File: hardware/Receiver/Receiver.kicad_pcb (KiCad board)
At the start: 4 copper layers, 65 x 42 mm, 98 parts, among them IC1 ESP32-C3-MINI-1-N4, J1 USB_C_Receptacle_USB2.0, J4 Conn_01x03, J5 20021511-00006T4LF, J6 Conn_01x04, Q1 2N7002, SW1 Reset, SW2 1825027-8, U1 DMG6602SVTQ, U2 DMG6602SVTQ, U3 TLV493DA1B6HTSA2, U4 TPS22810DRV, U5 TPS22810DRV, U6 AZ1117-3.3

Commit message: Removed old files
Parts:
- moved H4 2.35 mm to (134.5, 84.5)
- moved H2 2.35 mm to (165.6, 84.5)

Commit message: Revision 1.2 of receiver board
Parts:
- removed C1: 0.1u, Capacitor_SMD:C_0402_1005Metric
- D3: value D -> 1N4148WQ-13-F; footprint Capacitor_SMD:C_0402_1005Metric -> Diode_SMD:D_SOD-123
- D5: value D_Schottky -> EVVO SS16; footprint Diode_SMD:D_SOD-128 -> Diode_SMD:D_SMA
- moved J5 52.6 mm to (127.0, 83.3), turned to 0 degrees
- moved R15 48.0 mm to (180.0, 113.2), turned to -90 degrees
- moved U6 42.4 mm to (172.3, 116.4), turned to -90 degrees
- moved R6 42.0 mm to (167.2, 111.6), turned to 180 degrees
- moved Q1 41.9 mm to (177.7, 112.2), turned to 90 degrees
- moved R7 40.4 mm to (165.2, 111.6)
- moved R10 39.7 mm to (163.5, 110.2), turned to 180 degrees
- moved R21 38.0 mm to (171.4, 107.1), turned to 180 degrees
- moved C27 37.6 mm to (173.4, 111.4), turned to 0 degrees
- moved U1 37.0 mm to (166.4, 108.9), turned to 90 degrees
- moved SW1 36.9 mm to (136.6, 110.5), turned to 180 degrees
- moved D5 36.1 mm to (176.7, 108.4), turned to 0 degrees
- moved C25 35.8 mm to (171.1, 111.4), turned to 0 degrees
- moved D3 35.8 mm to (161.1, 108.4), turned to 0 degrees
- moved R13 35.0 mm to (164.0, 108.6), turned to -90 degrees
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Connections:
- IC1 pad 10: /DN_BTN -> /SHUTDOWN
- IC1 pad 11: unconnected-(IC1-IO32-Pad11) -> /DIR
- IC1 pad 12: unconnected-(IC1-IO33-Pad12) -> /STEP
- IC1 pad 13: unconnected-(IC1-IO25-Pad13) -> /MOT_nRST
- IC1 pad 14: unconnected-(IC1-IO26-Pad14) -> /MS3
- IC1 pad 15: unconnected-(IC1-IO27-Pad15) -> /MS2
- IC1 pad 16: unconnected-(IC1-IO14-Pad16) -> /MS1
- IC1 pad 25: /STEP -> unconnected-(IC1-IO9-Pad25)
- IC1 pad 26: /MOT_nRST -> unconnected-(IC1-IO10-Pad26)
- IC1 pad 29: /DIR -> unconnected-(IC1-IO5-Pad29)
- IC1 pad 34: /ADDRS_LED -> unconnected-(IC1-IO21-Pad34)
- IC1 pad 5: /MS3 -> unconnected-(IC1-I37-Pad5)
- IC1 pad 6: /MS2 -> unconnected-(IC1-I38-Pad6)
- IC1 pad 7: /MS1 -> unconnected-(IC1-I39-Pad7)
- IC1 pad 9: /UP_BTN -> /ADDRS_LED
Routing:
- net /SHUTDOWN: track 3.31 -> 47.4 mm
- net GND: track 154.7 -> 112.9 mm, vias 90 -> 95
- net /VUSB: track 53.7 -> 93.9 mm, vias 2 -> 5
- net /VSYS: track 8.26 -> 34.9 mm, vias 15 -> 7
- net /ESP_RX: track 33.0 -> 9.15 mm, vias 1 -> 0
- net /ESP_TX: track 30.4 -> 10.9 mm, vias 1 -> 0
- net /MOT_nEN: track 24.8 -> 40.9 mm
- net /STEP: track 27.0 -> 41.6 mm
- net /MS1: track 19.3 -> 33.6 mm
- net /MS2: track 19.6 -> 33.7 mm
- net /MS3: track 19.9 -> 33.8 mm
- net Net-(D3-K): track 25.9 -> 12.1 mm, vias 1 -> 0
- net /DIR: track 29.1 -> 42.8 mm
- net /SCL: track 13.4 -> 26.9 mm
- net /CNTRL: track 17.0 -> 6.09 mm, vias 4 -> 0
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- added copper zone on F.Cu, net +3.3V
- added copper zone on F.Cu, net /VIN
- removed copper zone on B.Cu, net /VSYS
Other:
- board text added: "JLCJLCJLCJLC"
- board text added: "REV 1.2.0"
- board text added: "STATUS"
- board text removed: "RESET"
- board text removed: "REV 1.0.0"

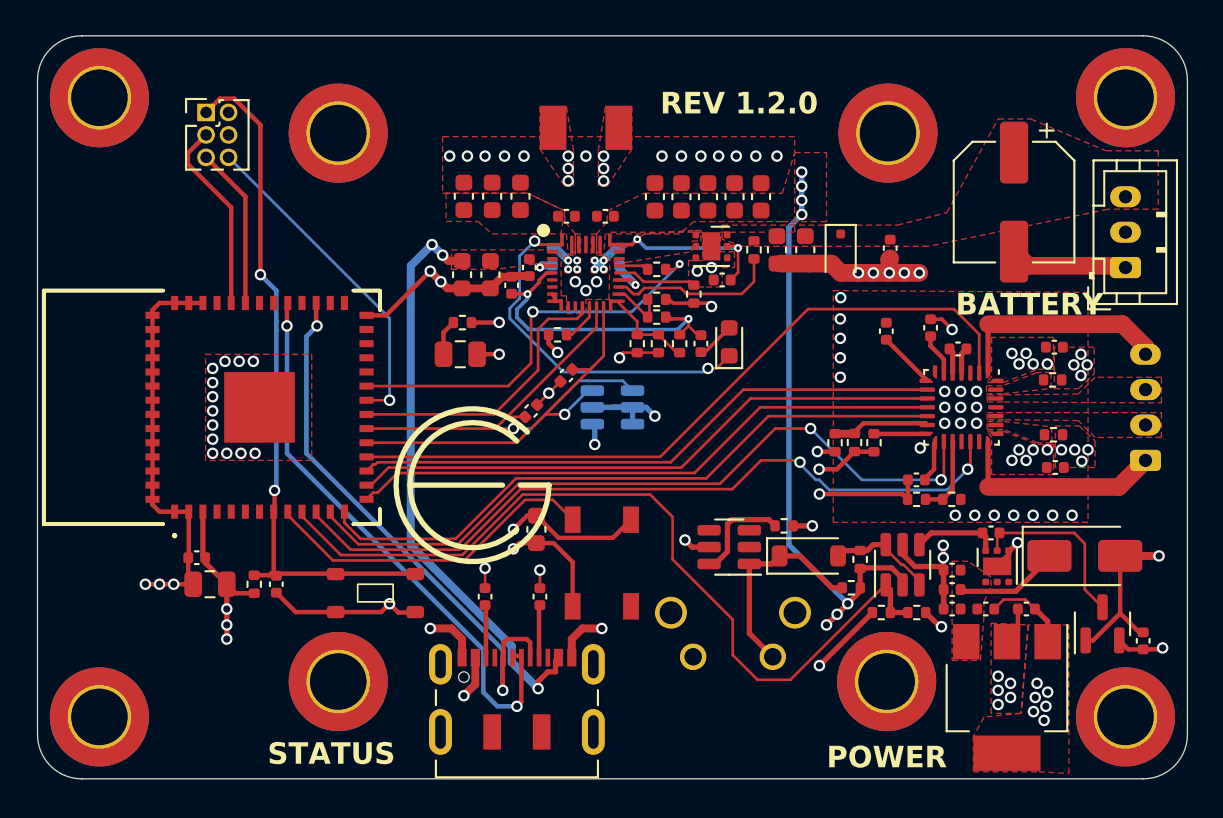
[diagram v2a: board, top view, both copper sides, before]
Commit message: BMS added to hardware
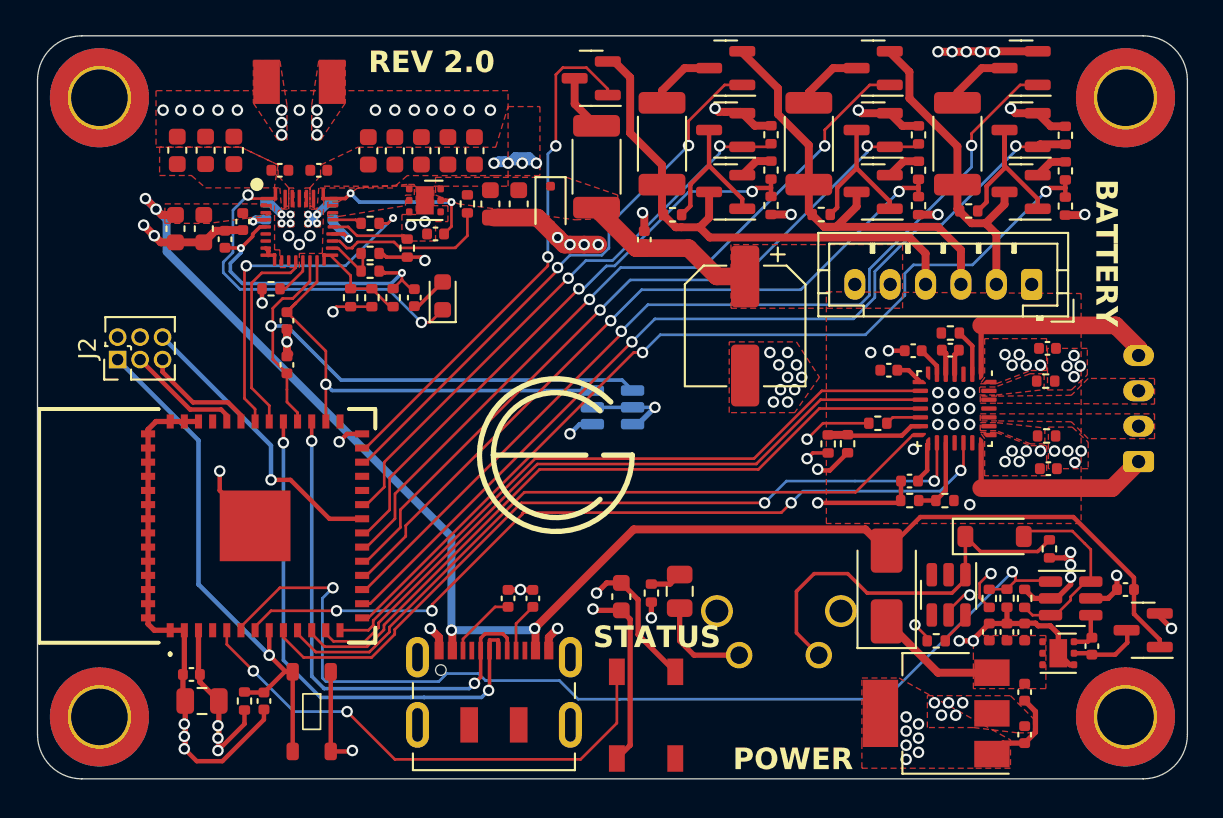
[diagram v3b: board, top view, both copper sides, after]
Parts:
- removed the C27 at (173.4, 111.4)
- removed the C32 at (126.5, 108.5)
- removed the C34 at (131.0, 110.0)
- removed the C7 at (145.7, 106.9)
- removed the D3 at (161.1, 108.4)
- removed the D5 at (176.7, 108.4)
- removed the H1 at (165.5, 115.5)
- removed the H2 at (165.6, 84.5)
- removed the H3 at (134.5, 115.5)
- removed the H4 at (134.5, 84.5)
- removed the J4 at (179.0, 92.1)
- removed J5: 20021511-00006T4LF, Connector_PinHeader_1.27mm:PinHeader_2x03_P1.27mm_Vertical
- removed the R10 at (163.5, 110.2)
- removed the R12 at (159.7, 106.7)
- removed the R13 at (164.0, 108.6)
- removed the R15 at (180.0, 113.2)
- removed the R2 at (142.8, 110.7)
- removed the R3 at (145.9, 110.7)
- removed the U1 at (166.4, 108.9)
- removed the U4 at (171.8, 109.0)
- added C21: 10u, Capacitor_SMD:C_0402_1005Metric, F.Cu at (173.3, 112.7)
- added C29: 47u, Capacitor_SMD:CP_Elec_6.3x5.4, F.Cu at (157.5, 95.4)
- added C33: 1u, Capacitor_SMD:C_0402_1005Metric, F.Cu at (130.3, 116.6)
- added C6: 10u, Capacitor_SMD:C_0603_1608Metric, F.Cu at (150.5, 110.7)
- added D4: 1N4148WQ-13-F, Diode_SMD:D_SOD-123, F.Cu at (171.6, 107.3)
- added D6: EVVO SS16, Diode_SMD:D_SMA, F.Cu at (165.5, 110.1)
- added J2: 20021511-00006T4LF, Connector_PinHeader_1.27mm:PinHeader_2x03_P1.27mm_Vertical, F.Cu at (122.0, 97.3)
- added J3: JST_PH, Connector_JST:JST_PH_B6B-PH-K_1x06_P2.00mm_Vertical, F.Cu at (173.7, 93.0)
- added Q10: NChan, Package_TO_SOT_SMD:SOT-23, F.Cu at (164.7, 80.8)
- added Q11: NChan, Package_TO_SOT_SMD:SOT-23, F.Cu at (173.1, 80.8)
- added Q2: NChan, Package_TO_SOT_SMD:SOT-23, F.Cu at (156.4, 84.3)
- added Q3: NChan, Package_TO_SOT_SMD:SOT-23, F.Cu at (164.7, 84.3)
- added Q4: NChan, Package_TO_SOT_SMD:SOT-23, F.Cu at (173.1, 84.3)
- added Q5: PChan, Package_TO_SOT_SMD:SOT-23, F.Cu at (156.4, 87.8)
- added Q6: PChan, Package_TO_SOT_SMD:SOT-23, F.Cu at (164.7, 87.8)
- added Q7: PChan, Package_TO_SOT_SMD:SOT-23, F.Cu at (173.1, 87.8)
- added Q8: NChan, Package_TO_SOT_SMD:SOT-23, F.Cu at (148.8, 81.4)
- added Q9: NChan, Package_TO_SOT_SMD:SOT-23, F.Cu at (156.4, 80.8)
- added R11: 100k, Resistor_SMD:R_0402_1005Metric, F.Cu at (168.3, 113.2)
- added R17: 100k, Resistor_SMD:R_0402_1005Metric, F.Cu at (173.3, 110.8)
- added R19: 100k, Capacitor_SMD:C_0402_1005Metric, F.Cu at (179.0, 110.3)
- added R20: 100k, Capacitor_SMD:C_0402_1005Metric, F.Cu at (177.1, 113.5)
- added R22: 100k, Resistor_SMD:R_0402_1005Metric, F.Cu at (167.3, 84.6)
- added R27: 282k, Resistor_SMD:R_0402_1005Metric, F.Cu at (159.0, 86.6)
- added R28: 100k, Resistor_SMD:R_0402_1005Metric, F.Cu at (159.0, 88.6)
- added R29: 155k, Resistor_SMD:R_0402_1005Metric, F.Cu at (167.3, 86.6)
- added R30: 100k, Resistor_SMD:R_0402_1005Metric, F.Cu at (167.3, 88.6)
- added R31: 28k, Resistor_SMD:R_0402_1005Metric, F.Cu at (175.6, 86.6)
- added R32: 100k, Resistor_SMD:R_0402_1005Metric, F.Cu at (175.6, 88.6)
- added R33: 400, Resistor_SMD:R_2010_5025Metric, F.Cu at (149.1, 86.4)
- added R34: 400, Resistor_SMD:R_2010_5025Metric, F.Cu at (152.8, 85.1)
- added R35: 400, Resistor_SMD:R_2010_5025Metric, F.Cu at (161.1, 85.1)
- added R36: 400, Resistor_SMD:R_2010_5025Metric, F.Cu at (169.5, 85.1)
- added R37: 100k, Resistor_SMD:R_0402_1005Metric, F.Cu at (169.1, 95.8)
- added R38: 100k, Resistor_SMD:R_0402_1005Metric, F.Cu at (165.0, 100.9)
- added R39: 10k, Capacitor_SMD:C_0402_1005Metric, F.Cu at (131.6, 95.1)
- added R40: 10k, Capacitor_SMD:C_0402_1005Metric, F.Cu at (131.6, 97.6)
- added R41: 10k, Resistor_SMD:R_0402_1005Metric, F.Cu at (129.2, 116.6)
- added R5: 5.1k, Capacitor_SMD:C_0402_1005Metric, F.Cu at (145.5, 110.8)
- added R8: 1M, Resistor_SMD:R_0402_1005Metric, F.Cu at (172.3, 110.8)
- added R9: 100k, Resistor_SMD:R_0402_1005Metric, F.Cu at (174.7, 108.0)
- added U3: DMG6602SVTQ, Package_TO_SOT_SMD:TSOT-23-6, F.Cu at (169.0, 110.6)
- added U5: TPS22810DRV, Package_SON:WSON-6-1EP_2x2mm_P0.65mm_EP1x1.6mm, F.Cu at (175.2, 113.9)
- C22: value 10u -> 1u
- C23: value 1u -> 0.1u
- C24: value 0.1u -> 10u
- C25: value 10u -> 10uf
- C26: value 10uf -> 22u
- C30: value 47u -> 22u; footprint Capacitor_SMD:CP_Elec_6.3x5.4 -> Capacitor_SMD:C_0805_2012Metric
- C31: value 22u -> 0.1u; footprint Capacitor_SMD:C_0805_2012Metric -> Capacitor_SMD:C_0402_1005Metric
- R21: footprint Capacitor_SMD:C_0402_1005Metric -> Resistor_SMD:R_0402_1005Metric
- R24, R25: value 10k -> 100k; footprint Capacitor_SMD:C_0402_1005Metric -> Resistor_SMD:R_0402_1005Metric
- R26: value 10k -> 100k
- R4: footprint Resistor_SMD:R_0402_1005Metric -> Capacitor_SMD:C_0402_1005Metric
- R6: value 100k -> 5.1k
- R7: value 1M -> 100k
- moved C30 53.9 mm to (126.8, 116.6), turned to 180 degrees
- moved R26 45.6 mm to (170.1, 88.9), turned to 0 degrees
- moved C26 28.5 mm to (173.3, 118.5)
- moved C25 28.4 mm to (151.8, 90.5), turned to 90 degrees
- moved R21 25.7 mm to (159.0, 84.6), turned to 90 degrees
- moved R23 20.5 mm to (175.6, 84.6)
- moved R25 19.8 mm to (161.8, 89.1), turned to 0 degrees
- moved U2 19.5 mm to (175.9, 110.8), turned to 0 degrees
- moved D2 18.3 mm to (153.8, 110.4), turned to 90 degrees
- moved D5 16.6 mm to (146.5, 88.6)
- moved C10 16.4 mm to (128.6, 85.5)
- moved C7 16.4 mm to (131.2, 86.6)
- moved R1 16.4 mm to (130.7, 93.3), turned to 180 degrees
- moved R13 16.4 mm to (137.6, 93.8)
- moved R14 16.4 mm to (135.2, 93.8)
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- renumbered C2 to C1, C11 to C10, C12 to C11, C13 to C12, C14 to C13, C20 to C14, C3 to C2, C21 to C20, C28 to C27, C29 to C28, C6 to C3, C33 to C32, C35 to C34, C36 to C35, C37 to C36, C8 to C7, C9 to C8, C10 to C9, D4 to D3, D6 to D5, H5 to H1, H6 to H2, H7 to H3, H8 to H4, J6 to J4, R5 to R1, R14 to R10, R16 to R12, R17 to R13, R18 to R14, R19 to R15, R20 to R16, R22 to R18, R8 to R2, R1 to R3, R27 to R42, R28 to R43, R29 to R44, R30 to R45, R31 to R46, R32 to R47, U5 to U1, U3 to U4
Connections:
- A1 pad 12: /MOT_nRST -> Net-(A1-nRESET)
- A1 pad 14: Net-(A1-nSLEEP) -> /MOT_nSLEEP
- A1 pad 2: /MOT_nEN -> Net-(A1-nEN)
- C25 pad 1: /VIN -> /BAT+
- C26 pad 1: /BAT+ -> +3.3V
- C30 pad 1: /BAT+ -> +3.3V
- IC1 pad 10: /SHUTDOWN -> /MOT_nSLEEP
- IC1 pad 11: /DIR -> /MS3
- IC1 pad 12: /STEP -> /MS2
- IC1 pad 13: /MOT_nRST -> /MS1
- IC1 pad 14: /MS3 -> /S4
- IC1 pad 15: /MS2 -> /M4
- IC1 pad 16: /MS1 -> /C4
- IC1 pad 17: /MOT_nEN -> /S3
- IC1 pad 18: /SDA -> /M3
- IC1 pad 19: /SCL -> /C3
- IC1 pad 20: /QON -> /S2
- IC1 pad 22: /BC_INT -> /M2
- IC1 pad 25: unconnected-(IC1-IO9-Pad25) -> /C2
- IC1 pad 26: unconnected-(IC1-IO10-Pad26) -> /C1
- IC1 pad 29: unconnected-(IC1-IO5-Pad29) -> /SDA
- IC1 pad 31: unconnected-(IC1-IO23-Pad31) -> /SCL
- IC1 pad 33: unconnected-(IC1-IO22-Pad33) -> /QON
- IC1 pad 34: unconnected-(IC1-IO21-Pad34) -> /BC_INT
- IC1 pad 5: unconnected-(IC1-I37-Pad5) -> /ADDRS_LED
- IC1 pad 6: unconnected-(IC1-I38-Pad6) -> /SHUTDOWN
- IC1 pad 7: unconnected-(IC1-I39-Pad7) -> /DIR
- IC1 pad 9: /ADDRS_LED -> /STEP
- R1 pad 1: GND -> /CE
- R1 pad 2: /CE -> GND
- R2 pad 1: /BC_INT -> /INT
- R2 pad 2: /INT -> /BC_INT
- R21 pad 1: Net-(Q1-D) -> /M2
- R21 pad 2: Net-(U1-D2) -> GND
- R23 pad 1: +3.3V -> /M4
- R23 pad 2: Net-(A1-nSLEEP) -> GND
- R24 pad 1: +3.3V -> /BAT_A
- R24 pad 2: /SDA -> Net-(Q2-D)
- R25 pad 1: +3.3V -> /BAT_B
- R25 pad 2: /SCL -> Net-(Q3-D)
- R26 pad 1: +3.3V -> /BAT_C
- R26 pad 2: /ESP_EN -> Net-(Q4-D)
- R4 pad 1: +3.3V -> Net-(J1-CC1)
- R4 pad 2: Net-(D2-A) -> GND
- R6 pad 2: /SHUTDOWN -> Net-(D2-A)
- R7 pad 1: /SHUTDOWN -> +3.3V
- R7 pad 2: GND -> /SHUTDOWN
- SW2 pad 2: Net-(D3-K) -> Net-(D4-K)
- U2 pad 1: Net-(D3-K) -> /SHUTDOWN
- U2 pad 2: unconnected-(U2-S2-Pad2) -> /VSYS
- U2 pad 3: unconnected-(U2-G2-Pad3) -> /CNTRL
- U2 pad 4: unconnected-(U2-D2-Pad4) -> Net-(U2-D2)
- U2 pad 6: Net-(U2-D1) -> /CNTRL
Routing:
- net /C4: track 0.00 -> 52.1 mm, vias 0 -> 2
- net /M4: track 0.00 -> 51.6 mm, vias 0 -> 2
- net /S4: track 0.00 -> 51.5 mm, vias 0 -> 2
- net /M3: track 0.00 -> 42.1 mm, vias 0 -> 2
- net /C3: track 0.00 -> 42.0 mm, vias 0 -> 2
- net /S3: track 0.00 -> 41.9 mm, vias 0 -> 2
- net /MOT_nSLEEP: track 0.00 -> 41.0 mm
- net /MOT_nEN: track 40.9 -> 0.00 mm
- net /VSYS: track 34.9 -> 72.8 mm
- net /MOT_nRST: track 36.8 -> 0.00 mm
- net /S2: track 0.00 -> 33.2 mm, vias 0 -> 2
- net /M2: track 0.00 -> 32.7 mm, vias 0 -> 2
- net /C2: track 0.00 -> 32.0 mm, vias 0 -> 2
- net /C1: track 0.00 -> 29.7 mm, vias 0 -> 2
- net /BAT_A: track 0.00 -> 29.4 mm
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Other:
- board text added: "REV 2.0"
- board text removed: "JLCJLCJLCJLC"
- board text removed: "REV 1.2.0"

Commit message: rename battery leads, update footprints
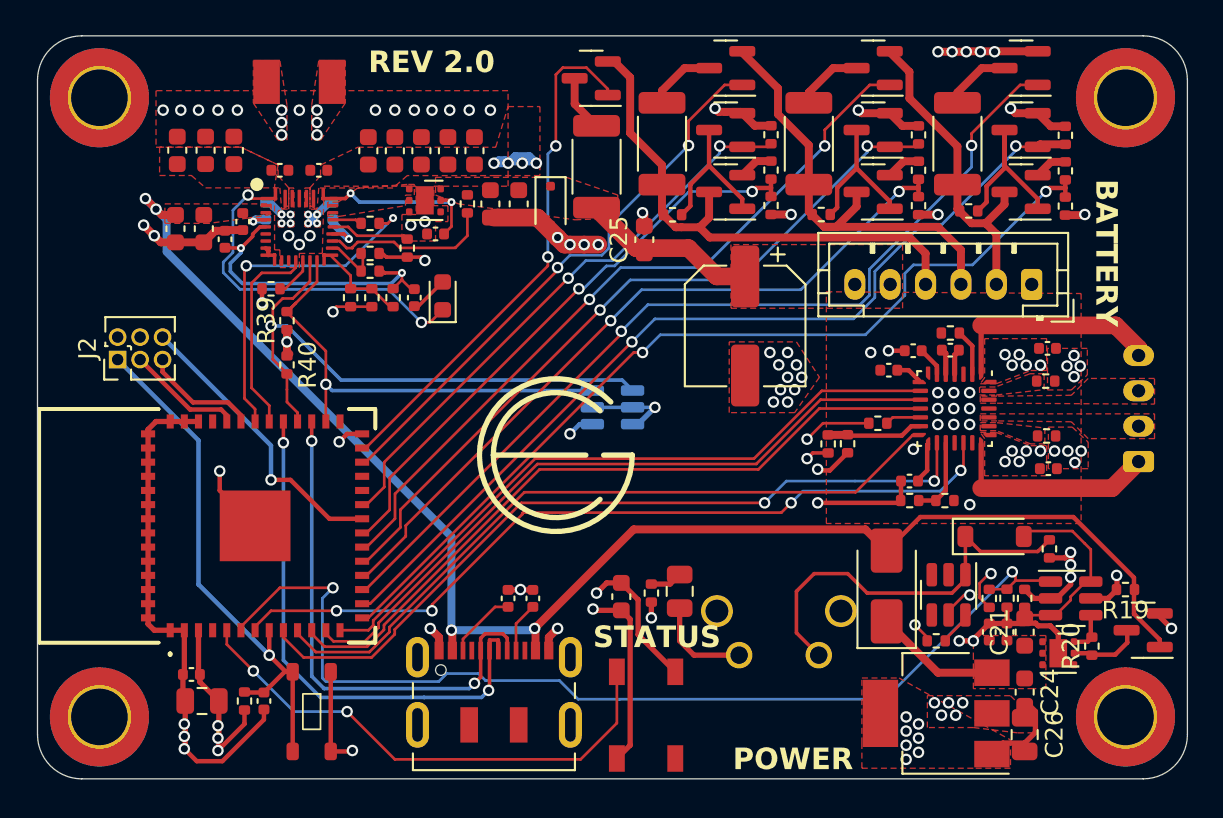
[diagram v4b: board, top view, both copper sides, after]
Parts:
- C14: value 1n -> NP
- C21, C24: footprint Capacitor_SMD:C_0402_1005Metric -> Capacitor_SMD:C_0603_1608Metric
- C25: value 10uf -> 10u; footprint Capacitor_SMD:C_0402_1005Metric -> Capacitor_SMD:C_0603_1608Metric
- C26: footprint Capacitor_SMD:C_0402_1005Metric -> Capacitor_SMD:C_0805_2012Metric
- R19, R20, R39, R40: footprint Capacitor_SMD:C_0402_1005Metric -> Resistor_SMD:R_0402_1005Metric
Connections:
- net /BAT_A renamed /BAT_C3
- net /BAT_B renamed /BAT_C2
- net /BAT_C renamed /BAT_C1
